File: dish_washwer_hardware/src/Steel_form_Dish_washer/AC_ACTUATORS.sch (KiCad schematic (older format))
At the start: 43 parts, among them J10 DRAIN PUMP CONNECTOR, J11 WASH PUMP CONNECTOR, J12 BOILER HEATER CONNECTOR, J13 TANK HEATER, J14 peristaltic_pump_2, J15 peristaltic_pump_1, J9 SOLENOID CONNECTOR, K1 9-1440003-0, K2 9-1440003-0, K3 9-1440003-0, Q3 WST2N7002K, Q4 WST2N7002K, Q5 WST2N7002K, U10 MOC3021, U11 MOC3021, U12 MOC3021, U7 MOC3021, U8 MOC3021, U9 MOC3021

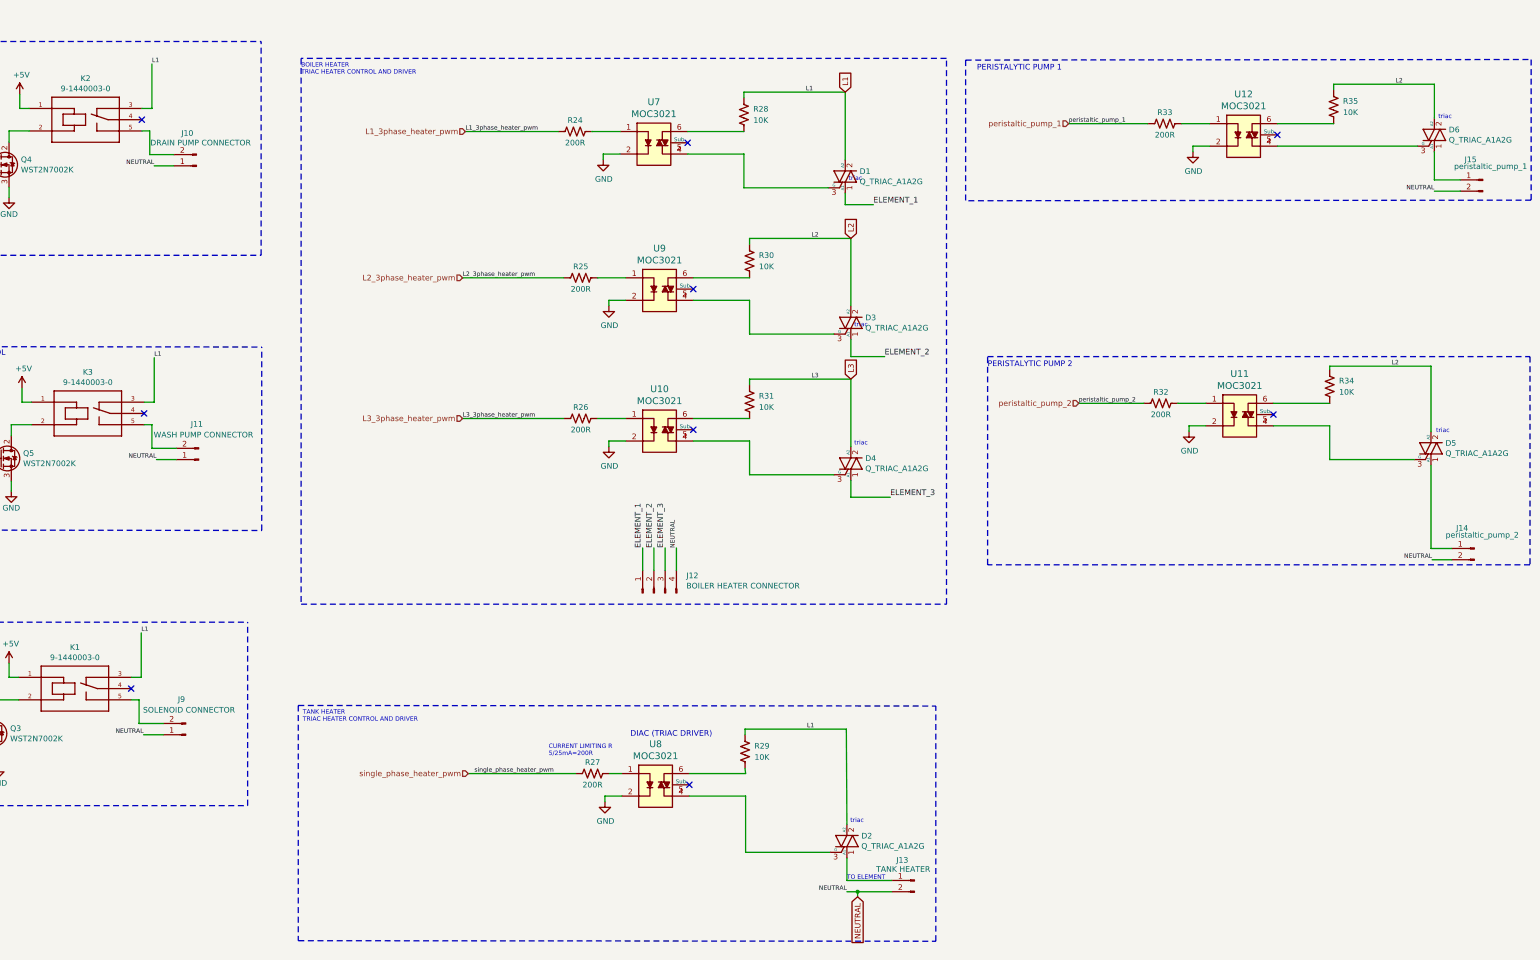
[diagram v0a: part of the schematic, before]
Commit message: footprint assignment and Varistor
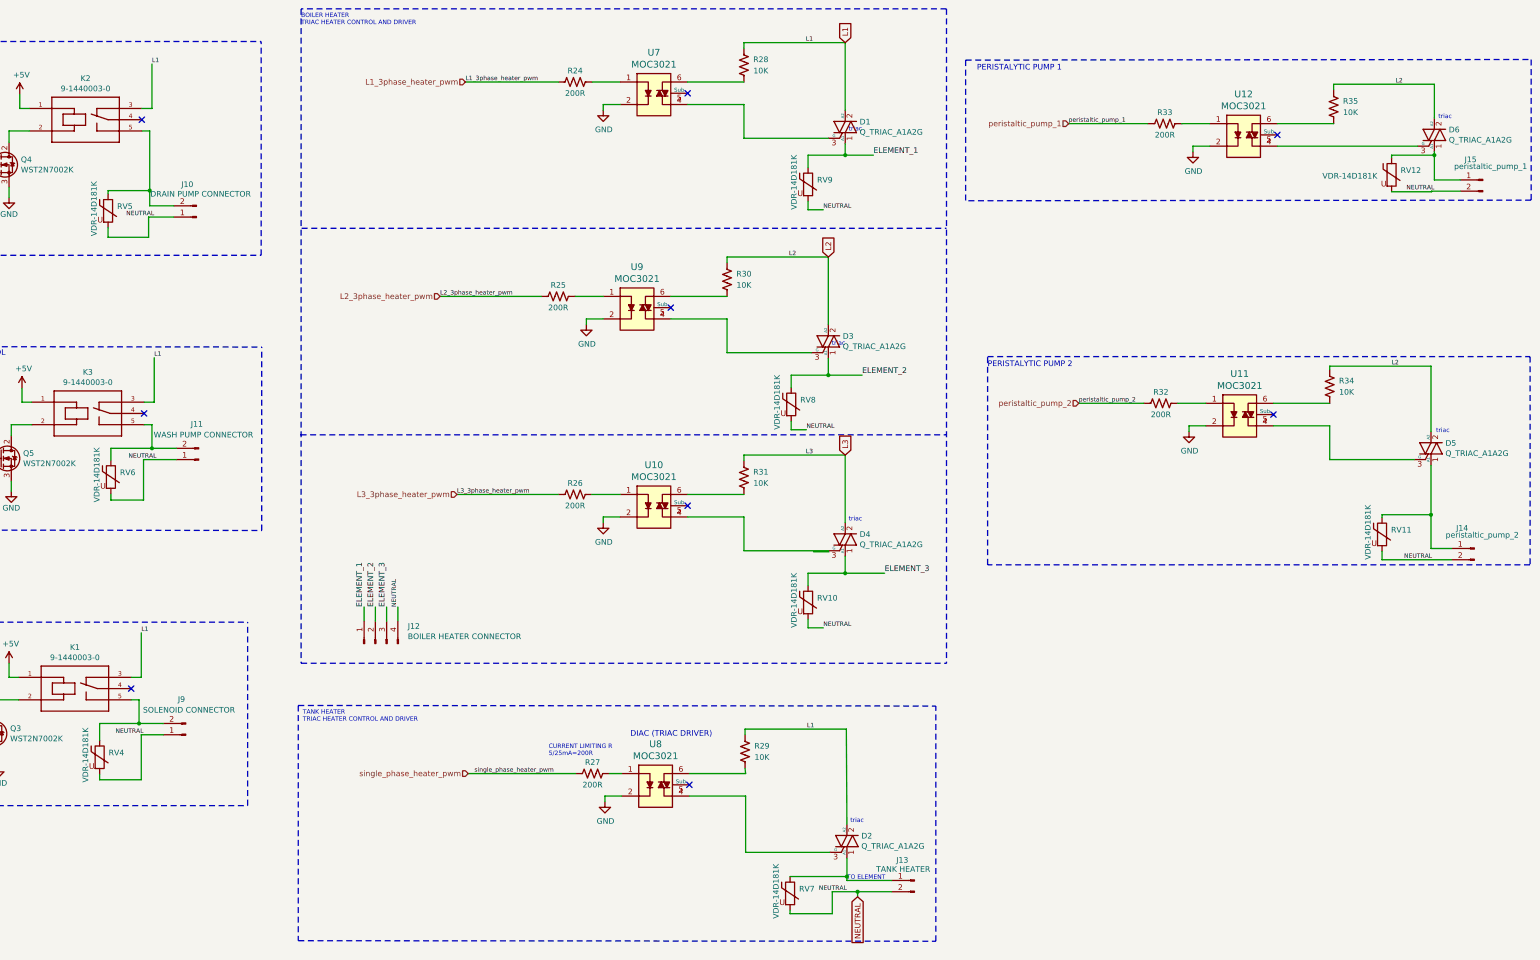
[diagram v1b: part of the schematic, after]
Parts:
- added RV10, RV11, RV12, RV4, RV5, RV6, RV7, RV8, RV9: VDR-14D181K, Varistor:RV_Disc_D16.5mm_W6.7mm_P7.5mm, symbol Device:Varistor
- J10: footprint (none) -> greencharge-footprints:SHDR2W100P0X508_1X2_1070X900X1380P; MPN (none) -> XY126V-5.0-2P
- J11, J14, J15, J9: footprint (none) -> greencharge-footprints:SHDR2W100P0X508_1X2_1070X900X1380P
- J12: footprint (none) -> greencharge-footprints:barrier_terminal_6PCV_04_006
- J13: footprint (none) -> greencharge-footprints:6PCV02006
- Q3, Q4, Q5: footprint (none) -> Package_TO_SOT_SMD:SOT-23
- R18, R19, R20, R21, R22, R23, R24, R25, R26, R27, R28, R29, R30, R31, R32, R33, R34, R35: footprint (none) -> Resistor_SMD:R_0402_1005Metric
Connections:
- net ELEMENT_1: now also RV9.1
- net ELEMENT_2: now also RV8.1
- net ELEMENT_3: now also RV10.1
- net NEUTRAL: now also RV10.2, RV11.2, RV12.2, RV4.2, RV5.2, RV6.2, RV7.2, RV8.2, RV9.2
- net at D2.1 (A1), J13.1 (Pin_1): now also RV7.1
- net at D5.1 (A1), J14.1 (Pin_1): now also RV11.1
- net at D6.1 (A1), J15.1 (Pin_1): now also RV12.1
- net at J9.2 (Pin_2), K1.5: now also RV4.1
- net at J10.2 (Pin_2), K2.5: now also RV5.1
- net at J11.2 (Pin_2), K3.5: now also RV6.1
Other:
- moved on the sheet: D1, D3, D4, J10, J12, R24, R25, R26, R28, R30, R31, U10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
